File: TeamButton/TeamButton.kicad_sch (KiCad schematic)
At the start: 5 parts, among them J1 RJ45, SW1 10T85 Microswitch, SW2 10T85 Microswitch

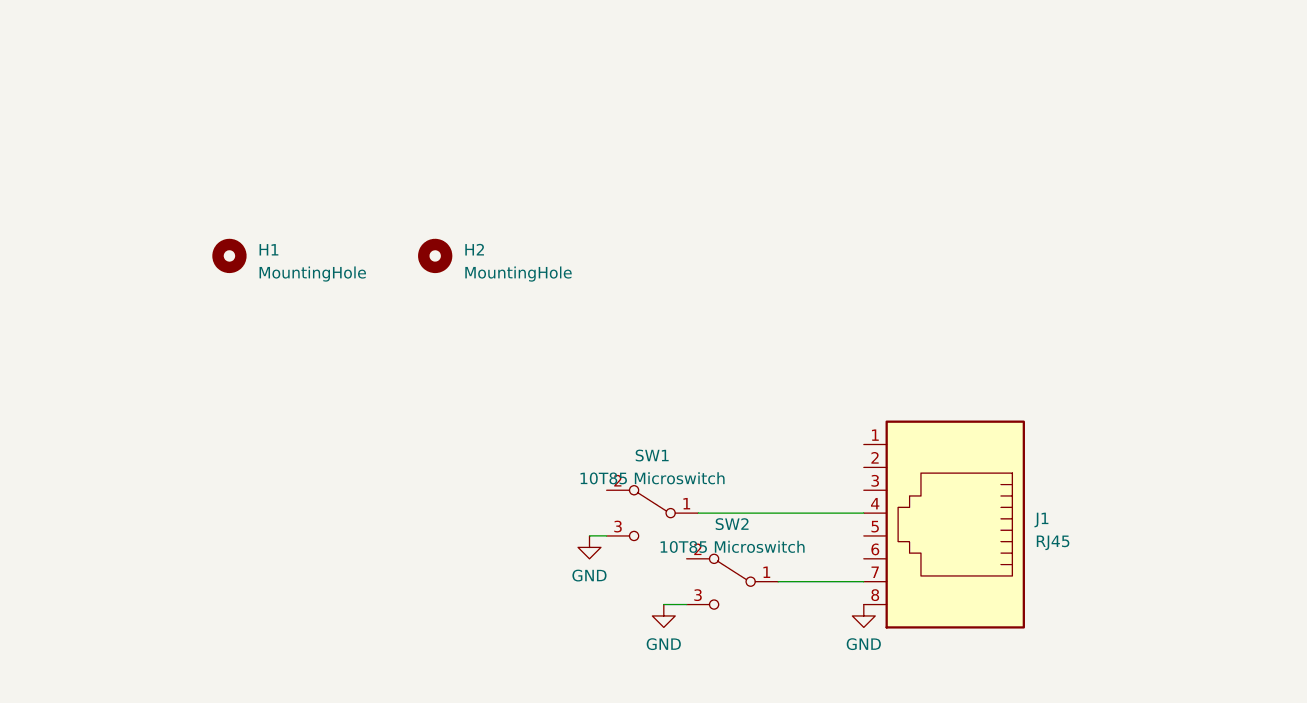
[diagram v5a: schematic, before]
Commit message: Added reset pins back in and broke out the pins in the team control area; should be easier now.  Yay!
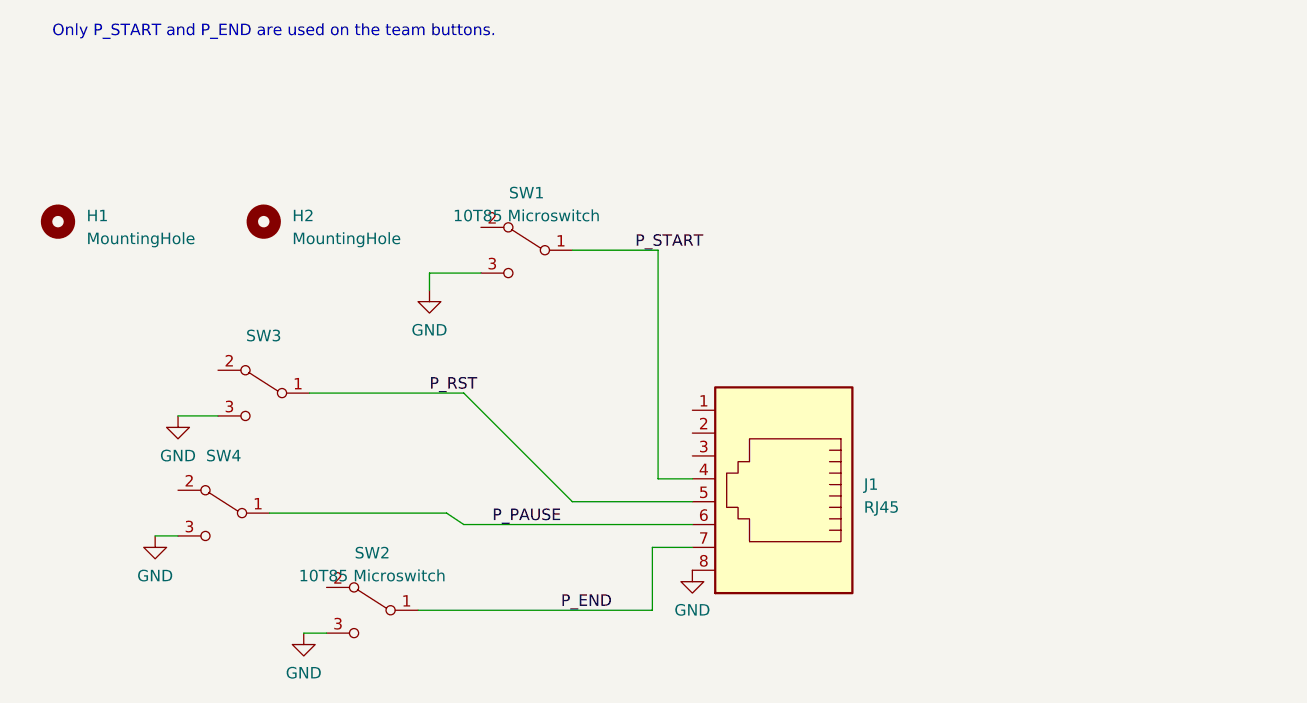
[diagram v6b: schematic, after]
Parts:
- added SW3, SW4: (no value), Connector_PinSocket_2.00mm:PinSocket_1x03_P2.00mm_Vertical, symbol symbols:10T85 Microswitch
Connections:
- net GND: now also SW3.3 (NO), SW4.3 (NO)
- net P_END: now reaches J1.7, SW2.1 (C)
- net P_START: now reaches J1.4, SW1.1 (C)
- net P_RST: now reaches J1.5
- net P_RST: now also SW3.1 (C)
- net P_PAUSE: now reaches J1.6
- net P_PAUSE: now also SW4.1 (C)
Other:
- note added: "Only P_START and P_END are used on the team buttons."
- company: (none) -> Garden State Combat Robotics League & FUBAR Labs
- title: (none) -> Team Button / Arena Control Buttons
- moved on the sheet: H1, H2, J1, SW1, SW2

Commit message: Release 7/19/23
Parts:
- removed SW3, SW4: (no value), Connector_PinSocket_2.00mm:PinSocket_1x03_P2.00mm_Vertical, symbol symbols:10T85 Microswitch
- added J2: Conn_01x08_MountingPin, Connector_PinSocket_2.54mm:PinSocket_1x08_P2.54mm_Horizontal, symbol Connector_Generic_MountingPin:Conn_01x08_MountingPin
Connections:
- net GND: now also J2.8 (Pin_8)
- net P_END: now also J2.7 (Pin_7)
- net P_START: now also J2.4 (Pin_4)
- net at J1.1: now also J2.1 (Pin_1)
- net at J1.2: now also J2.2 (Pin_2)
- net at J1.3: now also J2.3 (Pin_3)
- net P_PAUSE: no longer names the net of J1.6
- net P_PAUSE: now also J2.6 (Pin_6)
- net P_RST: no longer names the net of J1.5
- net P_RST: now also J2.5 (Pin_5)

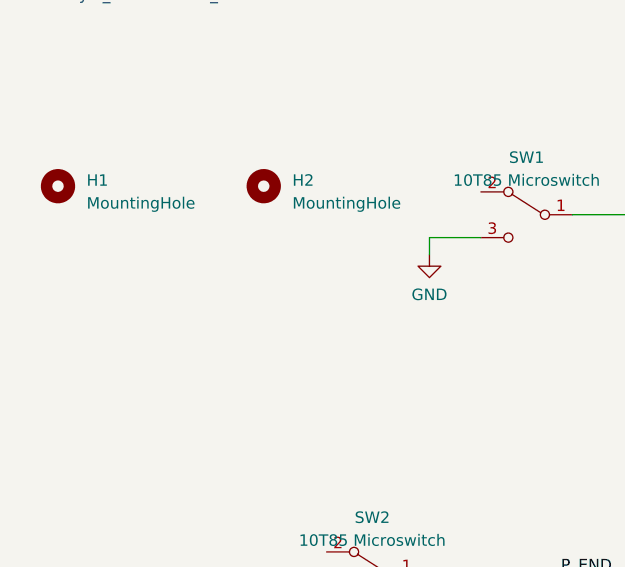
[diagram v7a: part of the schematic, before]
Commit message: Changed output tool to fix missing drill files, at least in theory.
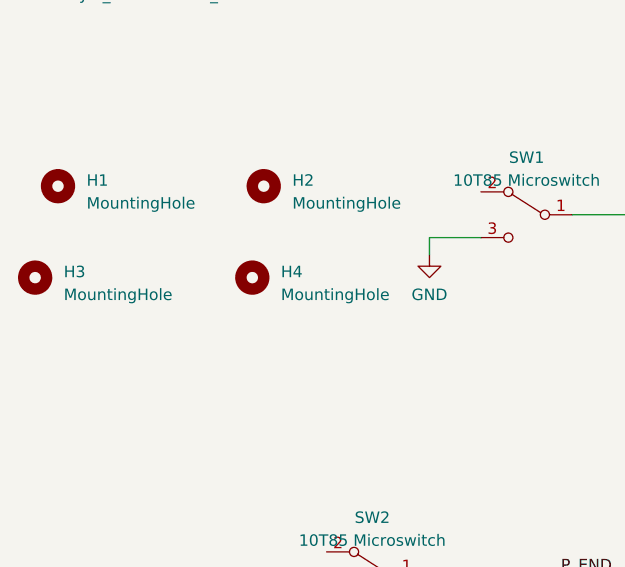
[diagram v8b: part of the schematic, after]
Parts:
- added H3, H4: MountingHole, MountingHole:MountingHole_3.2mm_M3, symbol Mechanical:MountingHole
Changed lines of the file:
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@@
+    )
+  )
+  (symbol (lib_id "Mechanical:MountingHole") (at 57.785 59.055 0) (unit 1)
+    (in_bom yes) (on_board yes) (dnp no) (fields_autoplaced)
+    (property "Reference" "H3" (at 60.96 58.42 0)
+      (effects (font (size 1.27 1.27)) (justify left))
+    )
+    (property "Value" "MountingHole" (at 60.96 60.96 0)
+      (effects (font (size 1.27 1.27)) (justify left))
+    )
+    (property "Footprint" "MountingHole:MountingHole_3.2mm_M3" (at 57.785 59.055 0)
+      (effects (font (size 1.27 1.27)) hide)
+    )
+    (property "Datasheet" "~" (at 57.785 59.055 0)
+      (effects (font (size 1.27 1.27)) hide)
+    )
+    (instances
+      (project "TeamButton"
+        (path "/a2251e9b-34a9-4b44-9287-d557388f6936"
+          (reference "H3") (unit 1)
+        )
+      )
     )
   )
@@
         )
       )
+    )
+  )
+  (symbol (lib_id "Mechanical:MountingHole") (at 81.915 59.055 0) (unit 1)
+    (in_bom yes) (on_board yes) (dnp no) (fields_autoplaced)
+    (property "Reference" "H4" (at 85.09 58.42 0)
+      (effects (font (size 1.27 1.27)) (justify left))
+    )
+    (property "Value" "MountingHole" (at 85.09 60.96 0)
+      (effects (font (size 1.27 1.27)) (justify left))
+    )
+    (property "Footprint" "MountingHole:MountingHole_3.2mm_M3" (at 81.915 59.055 0)
+      (effects (font (size 1.27 1.27)) hide)
+    )
+    (property "Datasheet" "~" (at 81.915 59.055 0)
+      (effects (font (size 1.27 1.27)) hide)
+    )
+    (instances
+      (project "TeamButton"
+        (path "/a2251e9b-34a9-4b44-9287-d557388f6936"
+          (reference "H4") (unit 1)
+        )
+      )
